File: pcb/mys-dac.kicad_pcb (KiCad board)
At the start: 2 copper layers, 49 x 63.5 mm, 31 parts, among them J1 OLED, J2 Conn_02x20_Odd_Even, J3 Conn_02x20_Odd_Even, J4 DAC, J5 IO, J6 CONSOLE, U1 WM8805, U2 AP1117-ADJ, U3 ISO7321C, Y1 Crystal

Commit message: Almost completely routed
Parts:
- removed REF** (x4): MountingHole_2.5mm, MountingHole:MountingHole_2.5mm
- added C8: 100n, Capacitor_SMD:C_0805_2012Metric_Pad1.15x1.40mm_HandSolder, F.Cu at (-19.0, -4.50)
- added C9: 1u, Capacitor_SMD:C_0805_2012Metric_Pad1.15x1.40mm_HandSolder, F.Cu at (-11.5, -15.5)
- added D1: SS14-E3/61T, Diode_SMD:D_SMA_Handsoldering, F.Cu at (-2.50, -14.5)
- added F1: 2A, Fuse:Fuse_1812_4532Metric_Pad1.30x3.40mm_HandSolder, F.Cu at (3.00, -18.5)
- added FB1: Ferrite_Bead_Small, Inductor_SMD:L_0805_2012Metric_Pad1.15x1.40mm_HandSolder, F.Cu at (-8.00, -16.0)
- added H1: MountingHole_Pad, MountingHole:MountingHole_2.5mm_Pad, F.Cu at (4.23, 25.0)
- added H2: MountingHole_Pad, MountingHole:MountingHole_2.5mm_Pad, F.Cu at (-39.0, 19.9)
- added H3: MountingHole_Pad, MountingHole:MountingHole_2.5mm_Pad, F.Cu at (4.23, -25.0)
- added H4: MountingHole_Pad, MountingHole:MountingHole_2.5mm_Pad, F.Cu at (-39.0, -19.9)
- added J7: SPDIF, micro-match:TE_MICRO-MATCH_FOB.14P, F.Cu at (-30.0, 2.00)
- added J8: PWR_IN, Connector_JST:JST_XH_B2B-XH-A_1x02_P2.50mm_Vertical, F.Cu at (3.50, -13.0)
- added L1: 2.2µ, Inductor_SMD:L_Taiyo-Yuden_NR-50xx_HandSoldering, F.Cu at (-6.50, 3.00)
- C1: value C -> 22µ; footprint Capacitor_SMD:C_0805_2012Metric_Pad1.15x1.40mm_HandSolder -> Capacitor_SMD:C_1206_3216Metric_Pad1.42x1.75mm_HandSolder
- C2: value C -> 4.7µ; footprint Capacitor_SMD:C_0805_2012Metric_Pad1.15x1.40mm_HandSolder -> Capacitor_SMD:C_1206_3216Metric_Pad1.42x1.75mm_HandSolder
- C3, C5: value C -> 15p
- R2: value R -> 536k
- R3: value R -> 100k
- R4, R5: value R -> 4.7k
- U2: value AP1117-ADJ -> TLV62568DBV; footprint Package_TO_SOT_SMD:SOT-223-3_TabPin2 -> Package_TO_SOT_SMD:SOT-23-5
- Y1: value Crystal -> 12MHz
- moved J4 65.0 mm to (-30.5, 32.0)
- moved J2 49.0 mm to (0.00, -25.5)
- moved J3 49.0 mm to (0.00, 23.5)
- moved R1 44.9 mm to (-7.50, 16.0), turned to 270 degrees
- moved J5 42.6 mm to (-7.50, 32.0), turned to 0 degrees
- moved J1 42.6 mm to (3.50, 8.50), turned to 90 degrees
- moved C6 38.6 mm to (-22.5, 20.5), turned to 180 degrees
- moved C3 37.9 mm to (-11.5, -19.5)
- moved J6 35.7 mm to (-28.0, 16.5)
- moved U3 35.7 mm to (-20.5, 16.5)
- moved C7 35.6 mm to (-18.5, 20.5)
- moved R2 33.7 mm to (-7.00, 12.0), turned to 180 degrees
- moved C5 33.7 mm to (-26.5, -19.5), turned to 270 degrees
- moved Y1 32.1 mm to (-16.5, -19.5), turned to 180 degrees
- moved C1 26.5 mm to (-5.50, 8.00), turned to 180 degrees
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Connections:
- net IMX_ONOFF renamed Net-(J2-Pad32)
- net IMX_POR renamed Net-(J2-Pad34)
- C1 pad 2: Net-(C1-Pad2) -> GND
- J2 pad 38: Net-(J2-Pad38) -> SNVS_TAMPER8
- J3 pad 18: KPP_ROW5 -> Net-(J3-Pad18)
- J4 pad 1: Net-(J4-Pad1) -> GND
- J4 pad 2: Net-(J4-Pad2) -> +3V3
- J5 pad 1: KPP_COL5 -> GND
- J5 pad 10: IR -> ENC1
- J5 pad 11: PWM8_OUT -> ENC2
- J5 pad 13: ENC2 -> PWM8_OUT
- J5 pad 14: ENC1 -> PWM5_OUT
- J5 pad 15: Net-(J5-Pad15) -> IR
- J5 pad 16: Net-(J5-Pad16) -> SNVS_TAMPER8
- J5 pad 2: KPP_ROW6 -> +3V3
- J5 pad 3: KPP_COL6 -> KPP_COL5
- J5 pad 4: KPP_ROW7 -> KPP_ROW6
- J5 pad 5: KPP_ROW4 -> KPP_COL6
- J5 pad 6: KPP_COL4 -> KPP_ROW7
- J5 pad 7: KPP_COL7 -> KPP_ROW4
- J5 pad 8: KPP_ROW5 -> KPP_COL4
- J5 pad 9: PWM5_OUT -> KPP_COL7
- R10 pad 1: GND -> Net-(R10-Pad1)
- R10 pad 2: Net-(R10-Pad2) -> GND
- R2 pad 2: Net-(C1-Pad2) -> Net-(R2-Pad2)
- R3 pad 1: Net-(C1-Pad2) -> Net-(R2-Pad2)
- R4 pad 1: VDD -> +3V3
- R5 pad 1: VDD -> +3V3
- R6 pad 1: VDD -> +3V3
- R9 pad 1: VDD -> +3V3
- R9 pad 2: Net-(R10-Pad2) -> Net-(R10-Pad1)
- U1 pad 1: Net-(U1-Pad1) -> +3V3
- U1 pad 11: Net-(U1-Pad11) -> /PVDD
- U1 pad 12: Net-(U1-Pad12) -> GND
- U1 pad 28: Net-(U1-Pad28) -> GND
- U1 pad 9: Net-(R10-Pad2) -> Net-(R10-Pad1)
- U2 pad 1: Net-(C1-Pad2) -> +5V
- U2 pad 2: /+3.8V -> GND
- U2 pad 3: +5V -> Net-(L1-Pad1)
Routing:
- net +3V3: track 7.30 -> 165.2 mm, vias 0 -> 7
- net SNVS_TAMPER8: track 0.00 -> 71.4 mm
- net SDA: track 25.2 -> 90.1 mm, vias 0 -> 2
- net SCL: track 25.1 -> 85.6 mm
- net GND: track 2.12 -> 37.0 mm, vias 0 -> 28
- net WM8805_RESET: track 0.00 -> 34.1 mm, vias 0 -> 3
- net ENC1: track 32.7 -> 66.5 mm
- net ENC2: track 32.4 -> 63.4 mm
- net PWM7_OUT: track 37.1 -> 65.8 mm
- net IMX_SPDIF_IN: track 0.00 -> 27.5 mm
- net KPP_ROW5: track 27.0 -> 0.00 mm
- net PWM8_OUT: track 36.8 -> 63.6 mm
- net PWM5_OUT: track 47.4 -> 74.0 mm
- net /+3.8V: track 0.00 -> 25.6 mm, vias 0 -> 2
- net +5V: track 0.00 -> 25.1 mm, vias 0 -> 5
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- added copper zone on B.Cu, net +3V3
- added copper zone on F.Cu, net +3V3
- added copper zone on F.Cu, net +5V
- added copper zone on F.Cu, net /+3.8V
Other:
- board size 49 x 63.5 mm -> 49 x 64 mm
- net class supply added: clearance 0.2, trace_width 0.5, via_dia 0.8, via_drill 0.4

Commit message: Routing complete
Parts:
- moved R2 9.30 mm to (-1.50, 4.50), turned to 270 degrees
- moved R8 6.52 mm to (-25.5, -3.00), turned to 0 degrees
- moved R7 3.50 mm to (-11.5, -6.00), turned to 180 degrees
- moved R3 1.80 mm to (-12.0, 10.5)
- moved C4 1.50 mm to (-9.50, -8.00)
- moved R10 1.50 mm to (-9.50, -10.0)
- moved C3 1.41 mm to (-12.5, -20.5)
- moved Y1 1.04 mm to (-17.5, -19.5)
- moved C1 1.00 mm to (-5.50, 7.00)
- moved C2 1.00 mm to (-13.5, 5.50)
- moved L1 1.00 mm to (-6.50, 2.00)
- moved U2 1.00 mm to (-10.0, 7.00)
- moved C5 0.71 mm to (-27.0, -19.0)
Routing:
- net +5V: track 25.1 -> 61.4 mm
- net +3V3: track 165.2 -> 194.6 mm
- net SDA: track 90.1 -> 74.5 mm, vias 2 -> 3
- net SCL: track 85.6 -> 72.3 mm, vias 0 -> 3
- net /+3.8V: track 25.6 -> 13.5 mm
- net Net-(R2-Pad2): track 5.47 -> 16.8 mm
- net IMX_UART_RX: track 16.7 -> 27.7 mm
- net IMX_UART_TX: track 19.2 -> 29.1 mm
- net GND: track 37.0 -> 44.8 mm, vias 28 -> 45
- net ENC1: track 66.5 -> 62.3 mm
- net Net-(R8-Pad1): track 10.7 -> 13.9 mm
- net ENC2: track 63.4 -> 60.7 mm
- net OLED_DC: track 26.1 -> 28.4 mm, vias 1 -> 0
- net SNVS_TAMPER8: track 71.4 -> 73.2 mm
- net PWM7_OUT: track 65.8 -> 64.1 mm
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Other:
- board size 49 x 64 mm -> 48.3 x 64 mm
- rule via_min_size: 0.4 -> 0.6
- board text added: "MYS-DAC Schwermer 2019"

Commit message: Done routing
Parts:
- moved C6 0.50 mm to (-23.0, 20.5)
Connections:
- net IR renamed IR_IN
- net PWM5_OUT renamed RED_LED
- net PWM7_OUT renamed GREEN_LED
- net PWM8_OUT renamed IR_OUT
- net SNVS_TAMPER8 renamed PWR_BTN
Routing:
- net GND: track 44.8 -> 45.9 mm, vias 45 -> 41
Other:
- board text added: "+5V"
- board text added: "Console"
- board text added: "DAC"
- board text added: "Front Panel I/O"
- board text added: "MYS-DAC 2019 Schwermer"
- board text added: "OLED"
- board text added: "S/PDIF I/O"
- board text removed: "MYS-DAC Schwermer 2019"

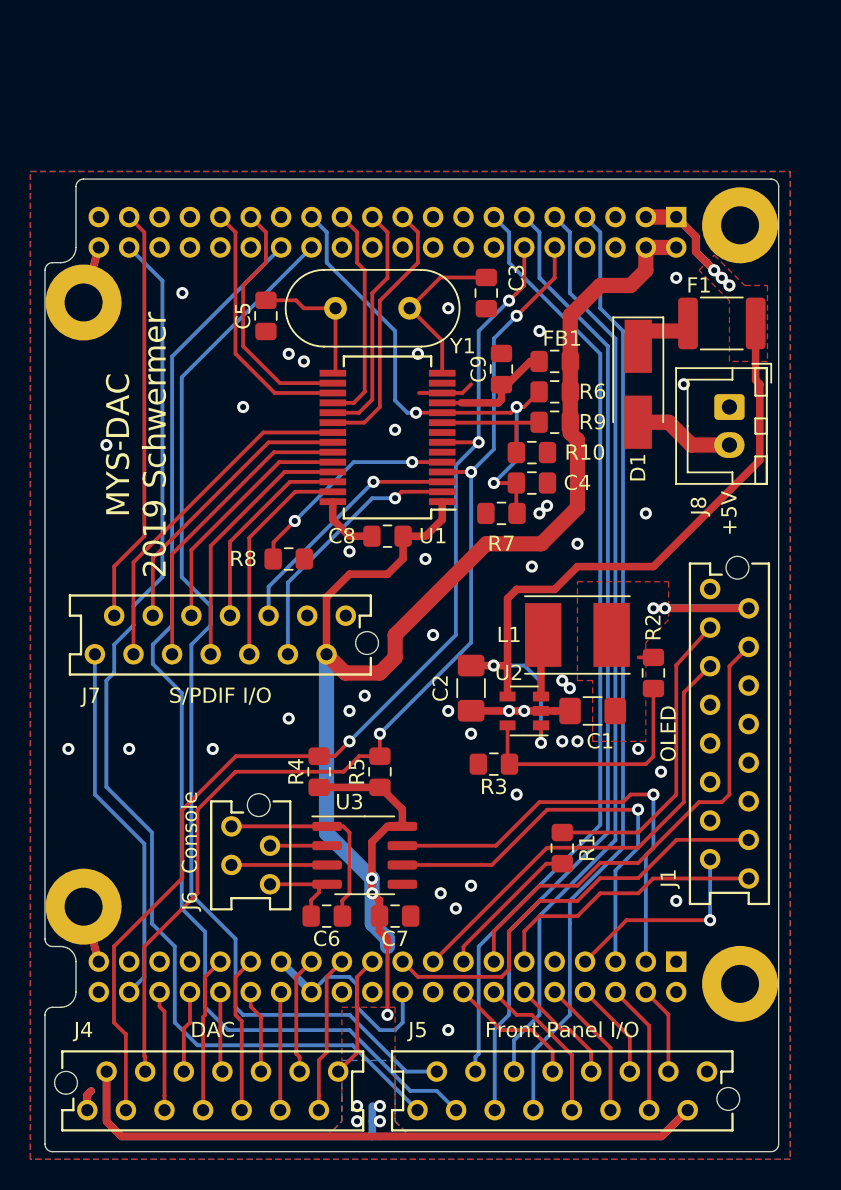
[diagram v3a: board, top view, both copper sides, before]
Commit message: PCBs sent to fab
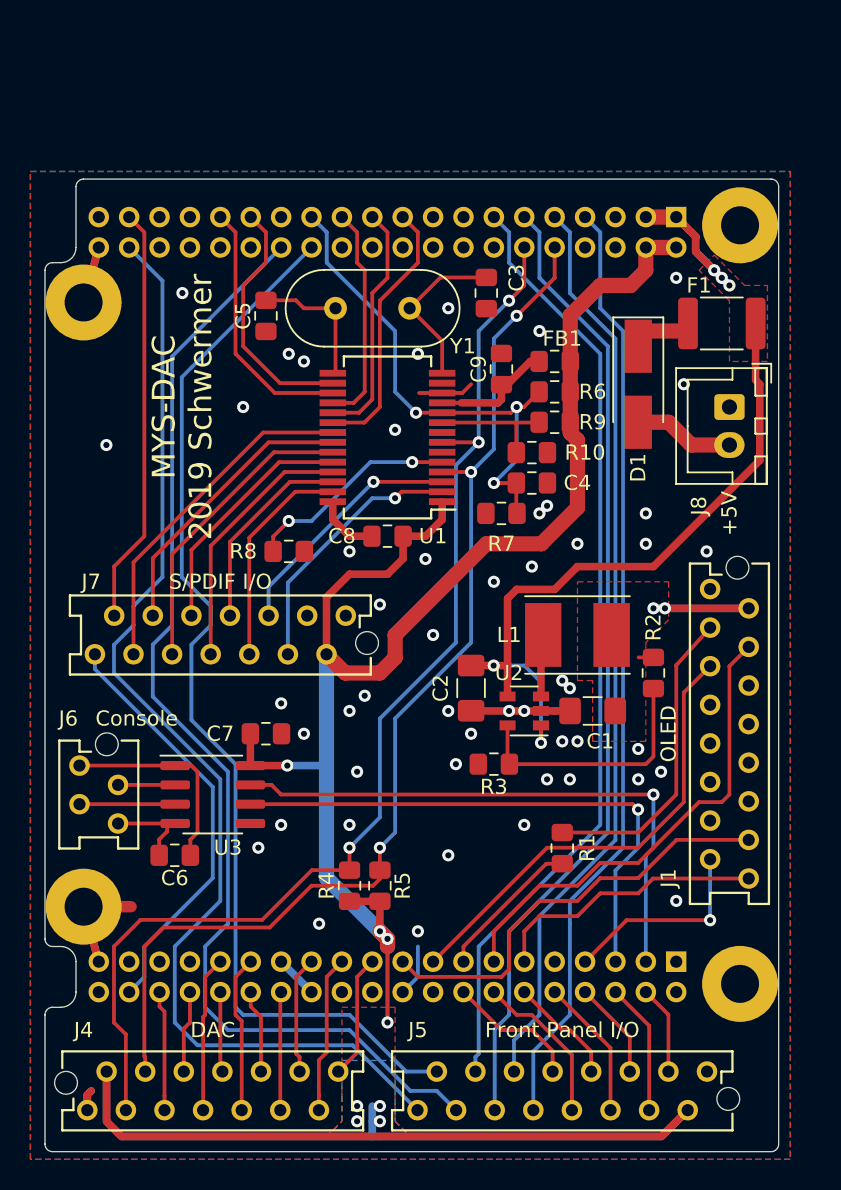
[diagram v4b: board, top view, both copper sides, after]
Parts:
- moved C7 14.7 mm to (-27.0, 8.50)
- moved C6 10.8 mm to (-33.0, 16.5)
- moved J6 10.8 mm to (-38.0, 12.5)
- moved U3 10.8 mm to (-30.5, 12.5)
- moved R4 7.76 mm to (-21.5, 18.5)
- moved R5 7.50 mm to (-19.5, 18.5)
- moved R8 0.50 mm to (-25.5, -3.50)
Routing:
- net IMX_UART_TX: track 29.1 -> 38.0 mm
- net IMX_UART_RX: track 27.7 -> 36.3 mm
- net GND: track 45.9 -> 41.5 mm, vias 41 -> 50
- net +3V3: track 194.6 -> 190.5 mm, vias 7 -> 8
- net IMX_SPDIF_OUT: track 24.0 -> 27.7 mm
- net SDA: track 74.5 -> 76.8 mm
- net PWR_BTN: track 73.7 -> 75.7 mm
- net SCL: track 72.3 -> 73.8 mm
- net RED_LED: track 74.2 -> 75.5 mm
